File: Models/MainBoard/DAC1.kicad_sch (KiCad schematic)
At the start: 2 parts, among them U4 DAC81404

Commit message: Finished the DACs
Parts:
- added C10, C12, C8: 10 uF, 0805, symbol Device:C
- added C11, C13, C7, C9: 100 nF, 0603, symbol Device:C
- added NT5, NT6, NT7, NT8: NetTie_2, symbol Device:NetTie_2
- added R6: 10k, 1%, symbol Device:R_US
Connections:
- net GND: now also U4.14 (GND), U4.29 (AGND), U4.33 (Thermal_pad), C10.1, C11.1, C12.1, C13.1, C7.1, C8.1, C9.1
- net OUTA: now reaches U4.1 (OUTA)
- net SCK: now reaches U4.10 (SCLK)
- net MOSI: now reaches U4.11 (SDIN)
- net CS: now reaches U4.12 (SYNC_N)
- net IOVDD: now reaches U4.13 (LDAC_N)
- net IOVDD: now also U4.15 (IOVDD), U4.16 (CLR_N), U4.32 (RST_N), C13.2, NT8.1, R6.1
- net OUTC: now reaches U4.17 (OUTC)
- net SENSEPC: now reaches U4.19 (SENSEPC)
- net SENSENC: now reaches U4.20 (SENSENC)
- net SENSEND: now reaches U4.21 (SENSEND)
- net SENSEPD: now reaches U4.22 (SENSEPD)
- net OUTD: now reaches U4.24 (OUTD)
- net AVSS: now reaches U4.27 (AVSS)
- net AVSS: now also C10.2, C9.2, NT6.1
- net AVDD: now reaches U4.28 (AVDD)
- net AVDD: now also C7.2, C8.2, NT5.1
- net SENSEPA: now reaches U4.3 (SENSEPA)
- net DVDD: now reaches U4.30 (DVDD)
- net DVDD: now also C11.2, C12.2, NT7.1
- net at U4.31 (FAULT_N): now also R6.2
- net SENSENA: now reaches U4.4 (SENSENA)
- net SENSENB: now reaches U4.5 (SENSENB)
- net SENSEPB: now reaches U4.6 (SENSEPB)
- net OUTB: now reaches U4.8 (OUTB)
- net MISO: now reaches U4.9 (SDO)
- new net -15V: NT6.2
- new net 15V: NT5.2
- new net 3.3V: NT8.2
- new net 5V: NT7.2
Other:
- note added: "For the piezo driver channels, the load (28k resistor) sits on a different board. Connect OUT, SENSEP, and SENSEN electrically closer to the target load resistor. Thus, SENSEN will use the ground potential at the target destination instead of the main board. TODO: Quantify the voltage difference between boards, due to both IR drops and magnetic induction."
- note removed: "For the piezo driver channels, the load (28k resistor) sits on a different board. Connect OUT, SENSEP, and SENSEN electrically closer to the target load resistor. Thus, SENSEN will use the ground potential at the target destination instead of the main board."
- note removed: "bypass caps (for both DACs): AVDD: 100 nF, 10 uF AVSS: 100 nF, 10 uF DVDD: 100 nF, 10 uF IOVDD: 100 nF"

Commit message: Save progress
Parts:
- removed NT5, NT6, NT7, NT8: NetTie_2, symbol Device:NetTie_2
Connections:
- net AVDD is gone; now on net 15V: C7.2, C8.2, U4.28 (AVDD)
- net AVSS is gone; now on net -15V: C10.2, C9.2, U4.27 (AVSS)
- net DVDD is gone; now on net 5V: C11.2, C12.2, U4.30 (DVDD)
- net IOVDD is gone; now on net 3.3V: C13.2, R6.1, U4.13 (LDAC_N), U4.15 (IOVDD), U4.16 (CLR_N), U4.32 (RST_N)

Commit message: Save progress
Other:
- note added: "For the piezo driver channels, the load (28k resistor) sits on a different board. We want the GND side of that resistor to sit at the same potential as the non-inverting input to the PA95 op amp. SENSEN detects the IR drop from difference in ground potentials (large power currents). Such currents do not flow through the SENSEN wire itself, thus IR drop is 0 across this one. SENSEP detects the sma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"
- note removed: "For the piezo driver channels, the load (28k resistor) sits on a different board. Connect OUT, SENSEP, and SENSEN electrically closer to the target load resistor. Thus, SENSEN will use the ground potential at the target destination instead of the main board. TODO: Quantify the voltage difference between boards, due to both IR drops and magnetic induction."
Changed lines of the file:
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@@
 	(generator_version "9.0")
 	(paper "A4")
-	(text "For the piezo driver channels, the load\n(28k resistor) sits on a different board.\nConnect OUT, SENSEP, and SENSEN electrically\ncloser to the target load resistor. Thus,\nSENSEN will use the ground potential at the\ntarget destination instead of the main board.\n\nTODO: Quantify the voltage difference between\nboards, due to both IR drops and magnetic\ninduction."
+	(text "For the piezo driver channels, the load\n(28k resistor) sits on a different board.\nWe want the GND side of that resistor to sit\nat the same potential as the non-inverting\ninput to the PA95 op amp.\n\nSENSEN detects the IR drop from difference in\nground potentials (large power currents). Such\ncurrents do not flow through the SENSEN wire\nitself, thus IR drop is 0 across this one.\n\nSENSEP detects the small IR drop from up to 428 uA\ncurrent flowing through the OUT wire. Current across\nSENSEP is (OUT wire resistance / 40k) * 428 uA.\n\nIn the worst case, 5 inches of 28 AWG wire are 0.027 Ω.\nVoltage drop is up to 11 μV. That is 1 part in 2 million\nerror with 24 V range. With 15 mA (35x higher current),\nit is 1 part in 60,000 and noticeable.\n\nWe do not need to utilize SENSEP for this particular\nDAC, avoiding much confusion and debugging. Only a\ndifferential + and - pairs for the voltage difference\nthat is transmitted between boards. OUT and SENSEN.\n\nTODO: Implement the above change."
 		(exclude_from_sim no)
-		(at 157.988 18.542 0)
+		(at 22.606 19.304 0)
 		(effects
 			(font

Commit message: Save progress
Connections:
- net SENSEPA is gone; now on net OUTA: U4.3 (SENSEPA)
- net SENSEPB is gone; now on net OUTB: U4.6 (SENSEPB)
- net SENSEPC is gone; now on net OUTC: U4.19 (SENSEPC)
- net SENSEPD is gone; now on net OUTD: U4.22 (SENSEPD)

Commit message: Save progress
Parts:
- added NT10, NT11, NT8, NT9: NetTie_2, symbol Device:NetTie_2
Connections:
- net -15V: now also NT9.2; no longer C10.2, C9.2, U4.27 (AVSS)
- net 15V: now also NT8.2; no longer C7.2, C8.2, U4.28 (AVDD)
- net 3.3V: now also NT11.2; no longer C13.2, R6.1, U4.13 (LDAC_N), U4.15 (IOVDD), U4.16 (CLR_N), U4.32 (RST_N)
- net 5V: now also NT10.2; no longer C11.2, C12.2, U4.30 (DVDD)
- new net AVDD: C7.2, C8.2, NT8.1, U4.28 (AVDD)
- new net AVSS: C10.2, C9.2, NT9.1, U4.27 (AVSS)
- new net DVDD: C11.2, C12.2, NT10.1, U4.30 (DVDD)
- new net IOVDD: C13.2, NT11.1, R6.1, U4.13 (LDAC_N), U4.15 (IOVDD), U4.16 (CLR_N), U4.32 (RST_N)

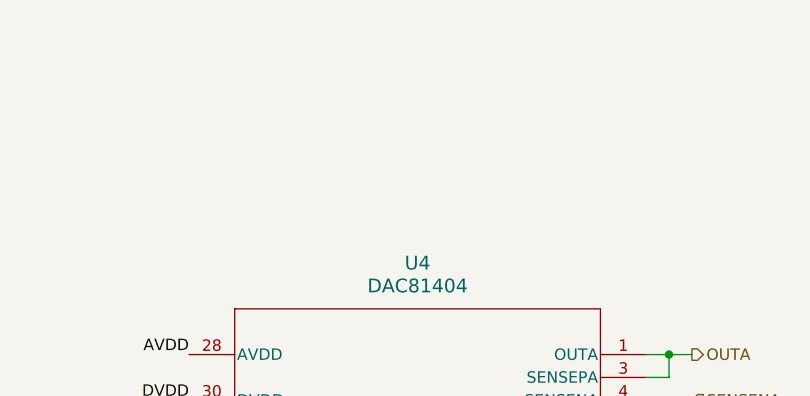
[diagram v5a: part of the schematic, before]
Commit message: Connectors should be fully specified now
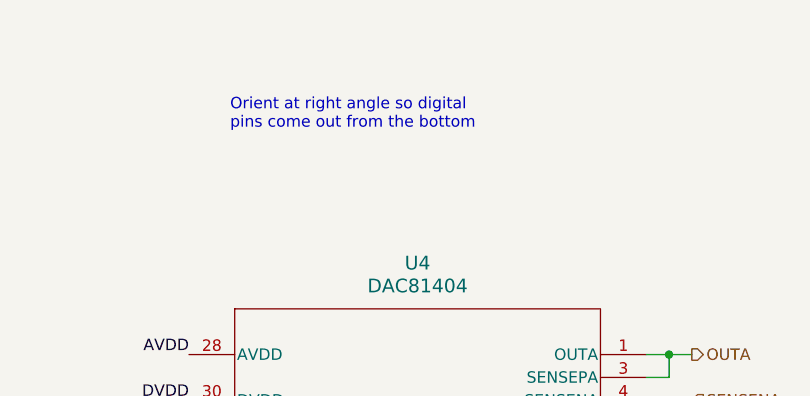
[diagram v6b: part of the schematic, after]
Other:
- note added: "Orient at right angle so digital pins come out from the bottom"
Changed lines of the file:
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@@
 	(generator_version "9.0")
 	(paper "A4")
+	(text "Orient at right angle so digital\npins come out from the bottom"
+		(exclude_from_sim no)
+		(at 111.252 27.432 0)
+		(effects
+			(font
+				(size 1.27 1.27)
+			)
+			(justify left top)
+		)
+	)
 	(text "For the piezo driver channels, the load\n(28k resistor) sits on a different board.\nWe want the GND side of that resistor to sit\nat the same potential as the non-inverting\ninput to the PA95 op amp.\n\nSENSEN detects the IR drop from difference in\nground potentials (large power currents). Such\ncurrents do not flow through the SENSEN wire\nitself, thus IR drop is 0 across this one.\n\nSENSEP detects the small IR drop from up to 428 uA\ncurrent flowing through the OUT wire. Current across\nSENSEP is (OUT wire resistance / 40k) * 428 uA.\n\nIn the worst case, 5 inches of 28 AWG wire are 0.027 Ω.\nVoltage drop is up to 11 μV. That is 1 part in 2 million\nerror with 24 V range. With 15 mA (35x higher current),\nit is 1 part in 60,000 and noticeable.\n\nWe do not need to utilize SENSEP for this particular\nDAC, avoiding much confusion and debugging. Only a\ndifferential + and - pair for the voltage difference\nthat is transmitted between boards. OUT and SENSEN."
 		(exclude_from_sim no)

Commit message: Passes ERC
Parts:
- renumbered C6 to C10, C7 to C11, C8 to C12, C9 to C13, C10 to C14, C11 to C15, C12 to C16, C13 to C17, NT8 to NT4, NT9 to NT5, NT10 to NT6, NT11 to NT7, U4 to U3
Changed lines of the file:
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@@
 		(dnp no)
 		(fields_autoplaced yes)
-		(property "Reference" "#PWR010"
+		(property "Reference" "#PWR045"
 			(at 196.85 50.8 0)
 			(effects
@@
 			(project ""
 				(path "/600cc1cc-74ca-4bfc-97a0-b230eb3afbcd/e222707b-78e5-4be0-8ce1-010f54f4492e"
-					(reference "#PWR010")
+					(reference "#PWR045")
 					(unit 1)
 				)
@@
 		(dnp no)
 		(fields_autoplaced yes)
-		(property "Reference" "#PWR07"
+		(property "Reference" "#PWR042"
 			(at 168.91 106.68 0)
 			(effects
@@
 			(project ""
 				(path "/600cc1cc-74ca-4bfc-97a0-b230eb3afbcd/e222707b-78e5-4be0-8ce1-010f54f4492e"
-					(reference "#PWR07")
+					(reference "#PWR042")
 					(unit 1)
 				)
@@
 		(dnp no)
 		(fields_autoplaced yes)
-		(property "Reference" "C10"
+		(property "Reference" "C14"
 			(at 217.17 81.28 90)
 			(effects
@@
 			(project "MainBoard"
 				(path "/600cc1cc-74ca-4bfc-97a0-b230eb3afbcd/e222707b-78e5-4be0-8ce1-010f54f4492e"
-					(reference "C10")
+					(reference "C14")
 					(unit 1)
 				)
@@
 		(dnp no)
 		(fields_autoplaced yes)
-		(property "Reference" "#PWR013"
+		(property "Reference" "#PWR048"
 			(at 196.85 127 0)
 			(effects
@@
 			(project "MainBoard"
 				(path "/600cc1cc-74ca-4bfc-97a0-b230eb3afbcd/e222707b-78e5-4be0-8ce1-010f54f4492e"
-					(reference "#PWR013")
+					(reference "#PWR048")
 					(unit 1)
 				)
@@
 		(dnp no)
 		(fields_autoplaced yes)
-		(property "Reference" "C6"
+		(property "Reference" "C10"
 			(at 92.71 114.2999 0)
 			(effects
@@
 			(project "MainBoard"
 				(path "/600cc1cc-74ca-4bfc-97a0-b230eb3afbcd/e222707b-78e5-4be0-8ce1-010f54f4492e"
-					(reference "C6")
+					(reference "C10")
 					(unit 1)
 				)
@@
 		(dnp no)
 		(fields_autoplaced yes)
-		(property "Reference" "NT8"
+		(property "Reference" "NT4"
 			(at 233.68 45.72 0)
 			(effects
@@
 			(project ""
 				(path "/600cc1cc-74ca-4bfc-97a0-b230eb3afbcd/e222707b-78e5-4be0-8ce1-010f54f4492e"
-					(reference "NT8")
+					(reference "NT4")
 					(unit 1)
 				)
@@
 		(dnp no)
 		(fields_autoplaced yes)
-		(property "Reference" "C7"
+		(property "Reference" "C11"
 			(at 217.17 43.18 90)
 			(effects
@@
 			(project ""
 				(path "/600cc1cc-74ca-4bfc-97a0-b230eb3afbcd/e222707b-78e5-4be0-8ce1-010f54f4492e"
-					(reference "C7")
+					(reference "C11")
 					(unit 1)
 				)
@@
 		(dnp no)
 		(fields_autoplaced yes)
-		(property "Reference" "NT10"
+		(property "Reference" "NT6"
 			(at 233.68 96.52 0)
 			(effects
@@
 			(project "MainBoard"
 				(path "/600cc1cc-74ca-4bfc-97a0-b230eb3afbcd/e222707b-78e5-4be0-8ce1-010f54f4492e"
-					(reference "NT10")
+					(reference "NT6")
 					(unit 1)
 				)
@@
 		(dnp no)
 		(fields_autoplaced yes)
-		(property "Reference" "U4"
+		(property "Reference" "U3"
 			(at 132.08 45.72 0)
 			(effects
@@
 			(project "MainBoard"
 				(path "/600cc1cc-74ca-4bfc-97a0-b230eb3afbcd/e222707b-78e5-4be0-8ce1-010f54f4492e"
-					(reference "U4")
+					(reference "U3")
 					(unit 1)
 				)
@@
 		(dnp no)
 		(fields_autoplaced yes)
-		(property "Reference" "#PWR011"
+		(property "Reference" "#PWR046"
 			(at 196.85 76.2 0)
 			(effects
@@
 			(project "MainBoard"
 				(path "/600cc1cc-74ca-4bfc-97a0-b230eb3afbcd/e222707b-78e5-4be0-8ce1-010f54f4492e"
-					(reference "#PWR011")
+					(reference "#PWR046")
 					(unit 1)
 				)
@@
 		(dnp no)
 		(fields_autoplaced yes)
-		(property "Reference" "C9"
+		(property "Reference" "C13"
 			(at 217.17 68.58 90)
 			(effects
@@
 			(project "MainBoard"
 				(path "/600cc1cc-74ca-4bfc-97a0-b230eb3afbcd/e222707b-78e5-4be0-8ce1-010f54f4492e"
-					(reference "C9")
+					(reference "C13")
 					(unit 1)
 				)
@@
 		(dnp no)
 		(fields_autoplaced yes)
-		(property "Reference" "C8"
+		(property "Reference" "C12"
 			(at 217.17 55.88 90)
 			(effects
@@
 			(project "MainBoard"
 				(path "/600cc1cc-74ca-4bfc-97a0-b230eb3afbcd/e222707b-78e5-4be0-8ce1-010f54f4492e"
-					(reference "C8")
+					(reference "C12")
 					(unit 1)
 				)
@@
 		(dnp no)
 		(fields_autoplaced yes)
-		(property "Reference" "#PWR08"
+		(property "Reference" "#PWR043"
 			(at 168.91 109.22 0)
 			(effects
@@
 			(project "MainBoard"
 				(path "/600cc1cc-74ca-4bfc-97a0-b230eb3afbcd/e222707b-78e5-4be0-8ce1-010f54f4492e"
-					(reference "#PWR08")
+					(reference "#PWR043")
 					(unit 1)
 				)
@@
 		(dnp no)
 		(fields_autoplaced yes)
-		(property "Reference" "#PWR012"
+		(property "Reference" "#PWR047"
 			(at 196.85 101.6 0)
 			(effects
@@
 			(project "MainBoard"
 				(path "/600cc1cc-74ca-4bfc-97a0-b230eb3afbcd/e222707b-78e5-4be0-8ce1-010f54f4492e"
-					(reference "#PWR012")
+					(reference "#PWR047")
 					(unit 1)
 				)
@@
 		(dnp no)
 		(fields_autoplaced yes)
-		(property "Reference" "C12"
+		(property "Reference" "C16"
 			(at 217.17 106.68 90)
 			(effects
@@
 			(project "MainBoard"
 				(path "/600cc1cc-74ca-4bfc-97a0-b230eb3afbcd/e222707b-78e5-4be0-8ce1-010f54f4492e"
-					(reference "C12")
+					(reference "C16")
 					(unit 1)
 				)
@@
 		(dnp no)
 		(fields_autoplaced yes)
-		(property "Reference" "C11"
+		(property "Reference" "C15"
 			(at 217.17 93.98 90)
 			(effects
@@
 			(project "MainBoard"
 				(path "/600cc1cc-74ca-4bfc-97a0-b230eb3afbcd/e222707b-78e5-4be0-8ce1-010f54f4492e"
-					(reference "C11")
+					(reference "C15")
 					(unit 1)
 				)
@@
 		(dnp no)
 		(fields_autoplaced yes)
-		(property "Reference" "C13"
+		(property "Reference" "C17"
 			(at 217.17 119.38 90)
 			(effects
@@
 			(project "MainBoard"
 				(path "/600cc1cc-74ca-4bfc-97a0-b230eb3afbcd/e222707b-78e5-4be0-8ce1-010f54f4492e"
-					(reference "C13")
+					(reference "C17")
 					(unit 1)
 				)
@@
 		(dnp no)
 		(fields_autoplaced yes)
-		(property "Reference" "NT9"
+		(property "Reference" "NT5"
 			(at 233.68 71.12 0)
 			(effects
@@
 			(project "MainBoard"
 				(path "/600cc1cc-74ca-4bfc-97a0-b230eb3afbcd/e222707b-78e5-4be0-8ce1-010f54f4492e"
-					(reference "NT9")
+					(reference "NT5")
 					(unit 1)
 				)
@@
 		(dnp no)
 		(fields_autoplaced yes)
-		(property "Reference" "#PWR03"
+		(property "Reference" "#PWR041"
 			(at 95.25 66.04 0)
 			(effects
@@
 			(project ""
 				(path "/600cc1cc-74ca-4bfc-97a0-b230eb3afbcd/e222707b-78e5-4be0-8ce1-010f54f4492e"
-					(reference "#PWR03")
+					(reference "#PWR041")
 					(unit 1)
 				)
@@
 		(dnp no)
 		(fields_autoplaced yes)
-		(property "Reference" "#PWR09"
+		(property "Reference" "#PWR044"
 			(at 168.91 119.38 0)
 			(effects
@@
 			(project ""
 				(path "/600cc1cc-74ca-4bfc-97a0-b230eb3afbcd/e222707b-78e5-4be0-8ce1-010f54f4492e"
-					(reference "#PWR09")
+					(reference "#PWR044")
 					(unit 1)
 				)
@@
 		(dnp no)
 		(fields_autoplaced yes)
-		(property "Reference" "#PWR04"
+		(property "Reference" "#PWR040"
 			(at 88.9 128.27 0)
 			(effects
@@
 			(project "MainBoard"
 				(path "/600cc1cc-74ca-4bfc-97a0-b230eb3afbcd/e222707b-78e5-4be0-8ce1-010f54f4492e"
-					(reference "#PWR04")
+					(reference "#PWR040")
 					(unit 1)
 				)
@@
 		(dnp no)
 		(fields_autoplaced yes)
-		(property "Reference" "NT11"
+		(property "Reference" "NT7"
 			(at 233.68 121.92 0)
 			(effects
@@
 			(project "MainBoard"
 				(path "/600cc1cc-74ca-4bfc-97a0-b230eb3afbcd/e222707b-78e5-4be0-8ce1-010f54f4492e"
-					(reference "NT11")
-					(unit 1)
-				)
+					(reference "NT7")
+					(unit 1)
+				)

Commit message: Save progress
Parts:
- U3: Cost (none) -> $41.54; Purchase Link (none) -> https://www.mouser.com/ProductDetail/Texas-Instruments/DAC8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
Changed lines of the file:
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@@
+			)
+		)
+		(property "Cost" "$41.54"
+			(at 132.08 86.36 0)
+			(effects
+				(font
+					(size 1.27 1.27)
+				)
+				(hide yes)
+			)
+		)
+		(property "Purchase Link" "https://www.mouser.com/ProductDetail/Texas-Instruments/DAC81404RHBT?qs=81r%252BiQLm7BQ4JX8PINPzgw%3D%3D"
+			(at 132.08 86.36 0)
+			(effects
+				(font
+					(size 1.27 1.27)
+				)
+				(hide yes)
 			)
 		)
